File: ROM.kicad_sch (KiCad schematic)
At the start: 11 parts, among them J2 WRITE PROTECT, U10 SST39SF040, U11 SST39SF040, U12 SST39SF040, U13 74AHC139, U9 SST39SF040

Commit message: added ATF150x part (specifically the 1508) vhdl file contains the (hopeful) implementition of the mapper
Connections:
- net ~{ROMEN0} renamed ~{ROM0}
- net ~{ROMEN_{1}} renamed ~{ROM_{1}}
- net ~{ROMEN_{2}} renamed ~{ROM_{2}}
- net ~{ROMEN_{3}} renamed ~{ROM_{3}}
- net ~{ROMEN} renamed ~{ROM}
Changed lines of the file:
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@@
     (effects (font (size 1.27 1.27)) (justify right bottom))
   )
-  (label "~{ROMEN_{2}}" (at 266.7 36.83 0)
+  (label "~{ROM_{2}}" (at 266.7 36.83 0)
     (effects (font (size 1.27 1.27)) (justify left bottom))
   )
@@
     (effects (font (size 1.27 1.27)) (justify right bottom))
   )
-  (label "~{ROMEN_{1}}" (at 266.7 34.29 0)
+  (label "~{ROM_{1}}" (at 266.7 34.29 0)
     (effects (font (size 1.27 1.27)) (justify left bottom))
   )
@@
     (effects (font (size 1.27 1.27)) (justify left bottom))
   )
-  (label "~{ROMEN_{1}}" (at 50.8 170.18 180)
+  (label "~{ROM_{1}}" (at 50.8 170.18 180)
     (effects (font (size 1.27 1.27)) (justify right bottom))
   )
@@
     (effects (font (size 1.27 1.27)) (justify right bottom))
   )
-  (label "~{ROMEN0}" (at 50.8 93.98 180)
+  (label "~{ROM0}" (at 50.8 93.98 180)
     (effects (font (size 1.27 1.27)) (justify right bottom))
   )
@@
     (effects (font (size 1.27 1.27)) (justify right bottom))
   )
-  (label "~{ROMEN_{2}}" (at 139.7 93.98 180)
+  (label "~{ROM_{2}}" (at 139.7 93.98 180)
     (effects (font (size 1.27 1.27)) (justify right bottom))
   )
@@
     (effects (font (size 1.27 1.27)) (justify left bottom))
   )
-  (label "~{ROMEN_{3}}" (at 139.7 170.18 180)
+  (label "~{ROM_{3}}" (at 139.7 170.18 180)
     (effects (font (size 1.27 1.27)) (justify right bottom))
   )
@@
     (effects (font (size 1.27 1.27)) (justify right bottom))
   )
-  (label "~{ROMEN_{3}}" (at 266.7 39.37 0)
+  (label "~{ROM_{3}}" (at 266.7 39.37 0)
     (effects (font (size 1.27 1.27)) (justify left bottom))
   )
@@
     (effects (font (size 1.27 1.27)) (justify right bottom))
   )
-  (label "~{ROMEN0}" (at 266.7 31.75 0)
+  (label "~{ROM0}" (at 266.7 31.75 0)
     (effects (font (size 1.27 1.27)) (justify left bottom))
   )
@@
     (effects (font (size 1.27 1.27)) (justify right))
   )
-  (hierarchical_label "~{ROMEN}" (shape input) (at 241.3 39.37 180)
-    (effects (font (size 1.27 1.27)) (justify right))
-  )
+  (hierarchical_label "~{ROM}" (shape input) (at 241.3 39.37 180)
+    (effects (font (size 1.27 1.27)) (justify right))
+  )

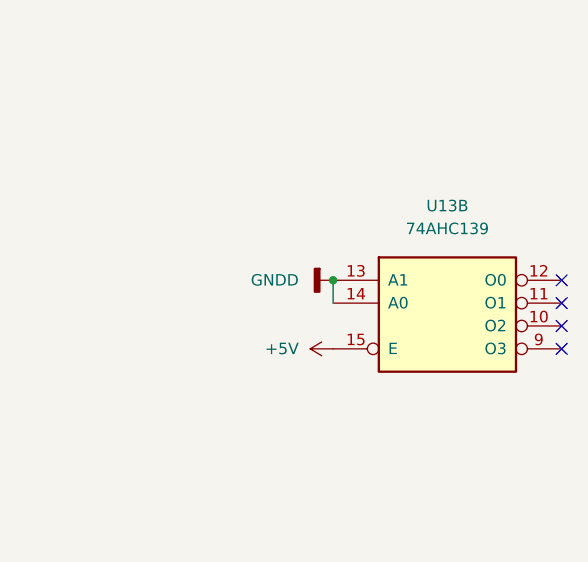
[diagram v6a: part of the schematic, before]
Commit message: updated 84c10 pinout, apparently never checked for validity.... further simplification of dma and timer system (removed mode 2 interrupt structure, and interrupts in general) cleaned up vhdl code for 1508, still need testing to ensure functionality and that it even fits in the 1508....
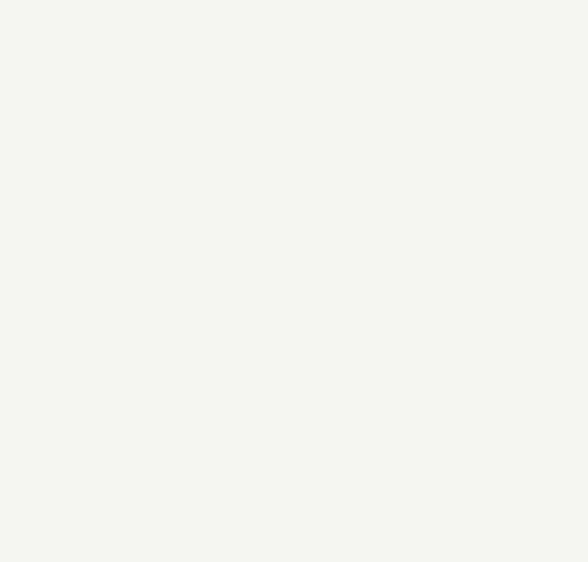
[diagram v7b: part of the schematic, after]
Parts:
- removed unit 2 of U13
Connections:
- no-connect marks 4 -> 0
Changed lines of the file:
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@@
     (comment 4 "rom is paged in on pages 4..127, and is in lower memory")
   )
-  (junction (at 254 152.4) (diameter 0) (color 0 0 0 0)
-  )
-  (no_connect (at 279.4 157.48))
-  (no_connect (at 279.4 154.94))
-  (no_connect (at 279.4 160.02))
-  (no_connect (at 279.4 152.4))
   (bus_entry (at 35.56 119.38) (size 2.54 2.54)
     (stroke (width 0) (type default) (color 0 0 0 0))
@@
   )
   (wire (pts (xy 127 154.94) (xy 139.7 154.94))
-    (stroke (width 0) (type default) (color 0 0 0 0))
-  )
-  (wire (pts (xy 254 152.4) (xy 254 154.94))
     (stroke (width 0) (type default) (color 0 0 0 0))
   )
@@
     (pin "1")
   )
-  (symbol (lib_id "power:GNDD") (at 254 152.4 270) (unit 1)
-    (in_bom yes) (on_board yes) (fields_autoplaced)
-    (property "Reference" "#PWR056" (id 0) (at 247.65 152.4 0)
-      (effects (font (size 1.27 1.27)) hide)
-    )
-    (property "Value" "GNDD" (id 1) (at 250.19 152.3999 90)
-      (effects (font (size 1.27 1.27)) (justify right))
-    )
-    (property "Footprint" "" (id 2) (at 254 152.4 0)
-      (effects (font (size 1.27 1.27)) hide)
-    )
-    (property "Datasheet" "" (id 3) (at 254 152.4 0)
-      (effects (font (size 1.27 1.27)) hide)
-    )
-    (pin "1")
-  )
   (symbol (lib_id "Device:C_Small") (at 168.275 172.72 0) (unit 1)
     (in_bom yes) (on_board yes) (fields_autoplaced)
@@
     )
     (pin "1")
-  )
-  (symbol (lib_id "power:+5V") (at 254 160.02 90) (unit 1)
-    (in_bom yes) (on_board yes) (fields_autoplaced)
-    (property "Reference" "#PWR057" (id 0) (at 257.81 160.02 0)
-      (effects (font (size 1.27 1.27)) hide)
-    )
-    (property "Value" "+5V" (id 1) (at 250.19 160.0199 90)
-      (effects (font (size 1.27 1.27)) (justify left))
-    )
-    (property "Footprint" "" (id 2) (at 254 160.02 0)
-      (effects (font (size 1.27 1.27)) hide)
-    )
-    (property "Datasheet" "" (id 3) (at 254 160.02 0)
-      (effects (font (size 1.27 1.27)) hide)
-    )
-    (pin "1")
-  )
-  (symbol (lib_id "74xx:74LS139") (at 266.7 154.94 0) (unit 2)
-    (in_bom yes) (on_board yes) (fields_autoplaced)
-    (property "Reference" "U13" (id 0) (at 266.7 144.145 0))
-    (property "Value" "74AHC139" (id 1) (at 266.7 146.685 0))
-    (property "Footprint" "Package_SO:TSSOP-16_4.4x5mm_P0.65mm" (id 2) (at 266.7 154.94 0)
-      (effects (font (size 1.27 1.27)) hide)
-    )
-    (property "Datasheet" "http://www.ti.com/lit/ds/symlink/sn74ls139a.pdf" (id 3) (at 266.7 154.94 0)
-      (effects (font (size 1.27 1.27)) hide)
-    )
-    (pin "1")
-    (pin "2")
-    (pin "3")
-    (pin "4")
-    (pin "5")
-    (pin "6")
-    (pin "7")
-    (pin "10")
-    (pin "11")
-    (pin "12")
-    (pin "13")
-    (pin "14")
-    (pin "15")
-    (pin "9")
-    (pin "16")
-    (pin "8")
   )
   (symbol (lib_id "74xx:74LS139") (at 254 34.29 0) (unit 1)
@@
   (symbol (lib_id "power:+5V") (at 255.27 83.82 0) (unit 1)
     (in_bom yes) (on_board yes) (fields_autoplaced)
-    (property "Reference" "#PWR058" (id 0) (at 255.27 87.63 0)
+    (property "Reference" "#PWR056" (id 0) (at 255.27 87.63 0)
       (effects (font (size 1.27 1.27)) hide)
     )
@@
   (symbol (lib_id "power:GNDD") (at 255.27 88.9 0) (unit 1)
     (in_bom yes) (on_board yes) (fields_autoplaced)
-    (property "Reference" "#PWR059" (id 0) (at 255.27 95.25 0)
-      (effects (font (size 1.27 1.27)) hide)
-    )
+    (property "Reference" "#PWR057" (id 0) (at 255.27 95.25 0)
+      (effects (font (size 1.27 1.27)) hide)
+    )
